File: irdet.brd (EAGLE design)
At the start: 50.8 x 47.9 mm, 66 parts, among them IC1 MEGA8-AI, IC2 78L05F, J1 PSH02-04WG, J2 PSH02-04WG, J3 PSH02-04WG, J4 PSH02-04WG, J5 22-05-7098-09, T1 S9013, T2 S9012, T3 S9013, T4 S9012, T5 S9013, T6 S9012, T7 S9013, T8 S9012, X1 ARK500/2

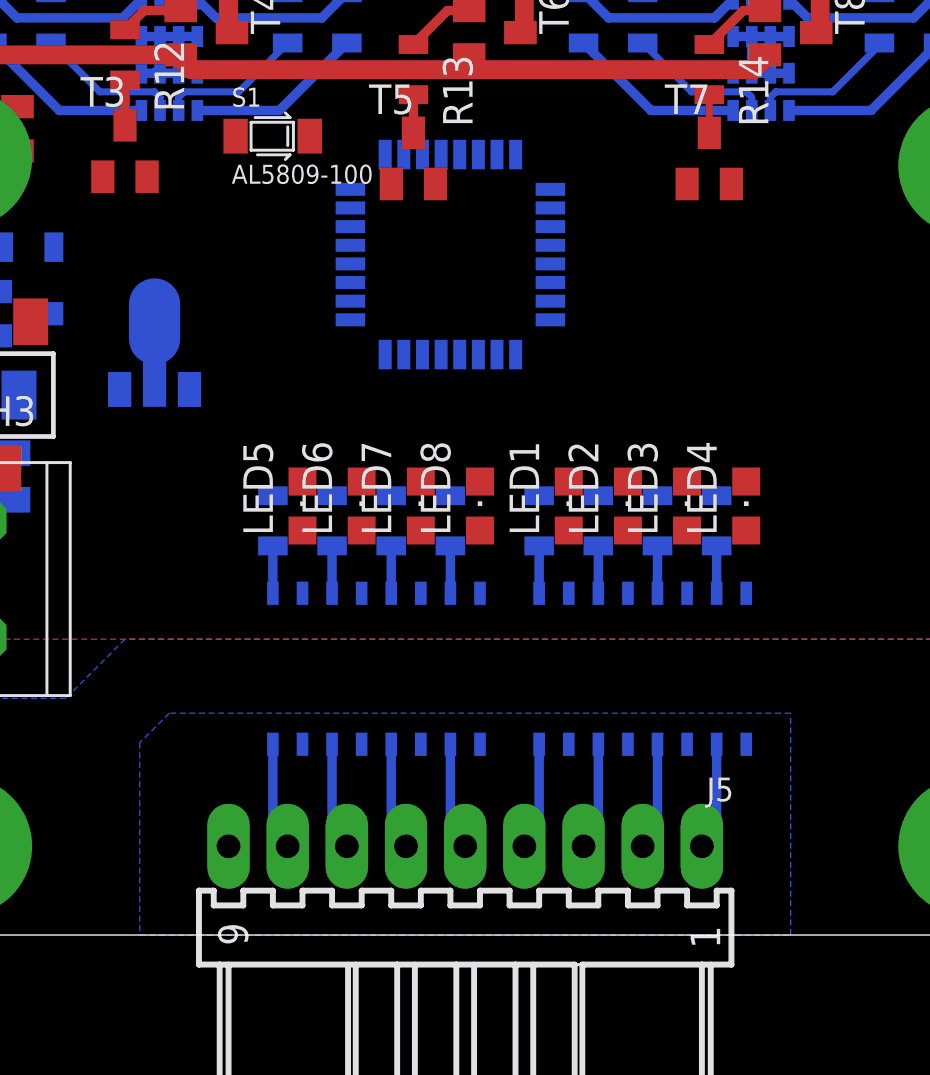
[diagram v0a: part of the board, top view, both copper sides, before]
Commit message: Rotate CPU.
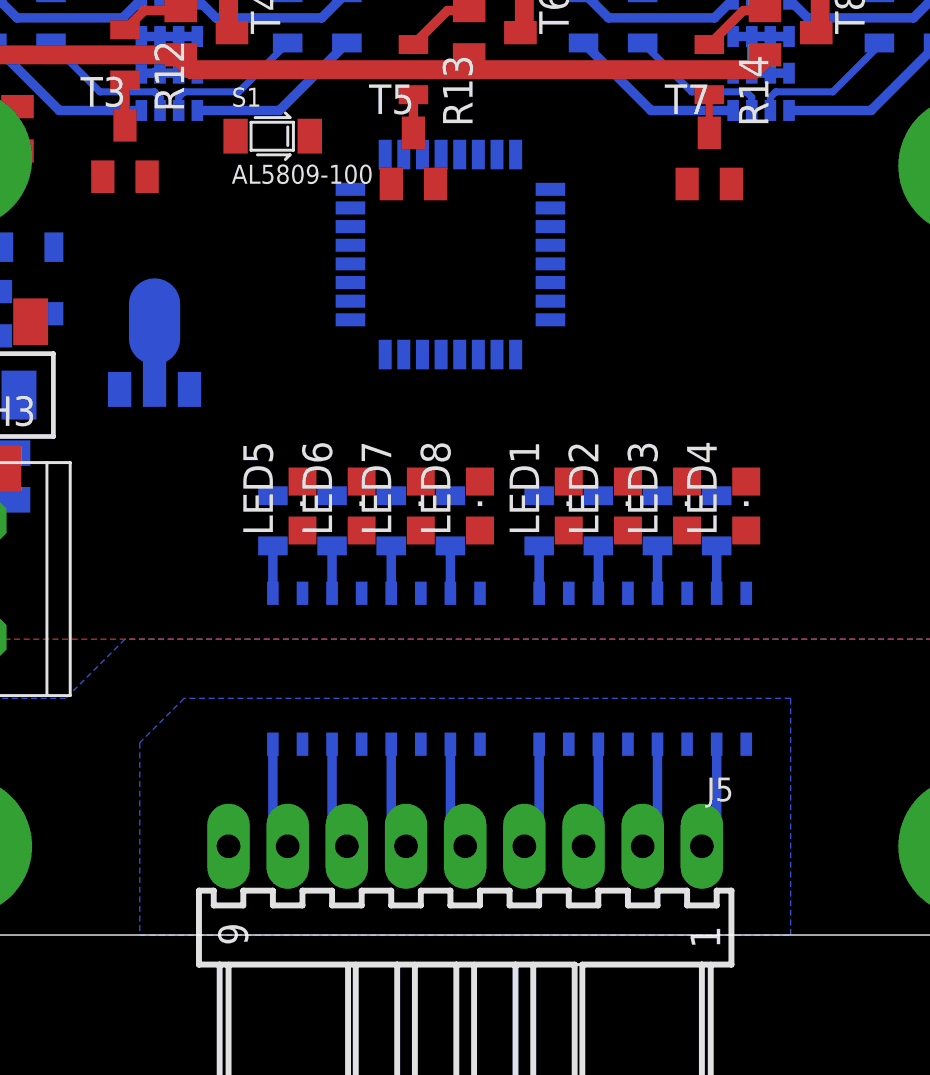
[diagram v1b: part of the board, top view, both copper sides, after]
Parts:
- turned IC1 to 0 degrees

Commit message: Add rest of PCB.
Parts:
- removed C3: 100n, rcl:C0805
- added X2: ARK500/2, con-malina:ARK500/2
- moved ISP1 43.8 mm to (39.4, 24.8), turned to 90 degrees
- moved R1 42.7 mm to (34.6, 27.9), flipped to the bottom, turned to 270 degrees
- moved C2 39.6 mm to (32.4, 27.9), flipped to the bottom, turned to 270 degrees
- moved C16 27.2 mm to (14.0, 28.9), turned to 180 degrees
- moved C1 24.3 mm to (18.4, 27.0), flipped to the bottom, turned to 270 degrees
- moved C8 15.3 mm to (7.94, 14.3), turned to 270 degrees
- moved C7 12.8 mm to (7.94, 18.1), turned to 270 degrees
- moved R2 9.55 mm to (11.7, 27.0), turned to 270 degrees
- moved TH3 9.38 mm to (12.7, 18.7)
- moved IC2 8.28 mm to (12.7, 17.1), turned to 90 degrees
- moved C13 7.73 mm to (9.84, 27.0), turned to 90 degrees
- moved T3 7.24 mm to (17.8, 31.8)
- moved R11 6.36 mm to (7.94, 34.3), turned to 315 degrees
- moved T1 6.11 mm to (10.5, 31.8), turned to 0 degrees
- moved C12 6.03 mm to (3.17, 25.7), turned to 0 degrees
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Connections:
- removed net MISO: IC1.16, ISP1.1
- removed net MOSI/IN7: C14.1, IC1.15, ISP1.4, RN4.2
- removed net N$34: F1.1, X1.1
- removed net OUT1: IC1.30, R3.1
- removed net OUT2: IC1.31, R4.1
- new net +12VIN: F1.1, X1.2, X2.1
- new net IN7: C14.1, IC1.32, RN4.2
- new net MISO/OUT1: IC1.16, ISP1.1, R7.1
- new net MOSI/OUT2: IC1.15, ISP1.4, R8.1
- net +5V: no longer C3.1
- net CPUPOW1-2: now also IC1.23; no longer IC1.12
- net CPUPOW3-4: now also IC1.24; no longer IC1.13
- net CPUPOW5-6: now also IC1.2; no longer IC1.14
- net GND: now also X1.1, X2.2; no longer C3.2, X1.2
- net IN1: now also IC1.25; no longer IC1.23
- net IN2: now also IC1.26; no longer IC1.24
- net IN3: now also IC1.28; no longer IC1.25
- net IN4: now also IC1.27; no longer IC1.26
- net IN5: now also IC1.31; no longer IC1.27
- net IN6: now also IC1.30; no longer IC1.28
- net IN8: now also IC1.1; no longer IC1.8
- net OUT3: now also IC1.14, R9.1; no longer IC1.32, R5.1
- net OUT4: now also IC1.13, R10.1; no longer IC1.1, R6.1
- net OUT5: now also IC1.12, R3.1; no longer IC1.2, R7.1
- net OUT6: now also IC1.11, R4.1; no longer IC1.9, R8.1
- net OUT7: now also R5.1; no longer R9.1
- net OUT8: now also IC1.9, R6.1; no longer IC1.11, R10.1
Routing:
- net +5V: track 12.8 -> 99.1 mm, vias 0 -> 8
- net +12VIN: track 0.00 -> 56.0 mm
- net MOSI/OUT2: track 0.00 -> 25.7 mm, vias 0 -> 1
- net MISO/OUT1: track 0.00 -> 25.2 mm, vias 0 -> 1
- net +12V: track 0.00 -> 24.8 mm, vias 0 -> 1
- net RST: track 0.00 -> 23.7 mm, vias 0 -> 2
- net SCK: track 0.00 -> 23.0 mm, vias 0 -> 1
- net IN7: track 0.00 -> 17.8 mm
- net IN2: track 6.21 -> 20.9 mm
- net CPUPOW1-2: track 0.00 -> 13.3 mm, vias 0 -> 1
- net IN1: track 7.62 -> 20.7 mm
- net CPUPOW7-8: track 0.00 -> 12.9 mm, vias 0 -> 1
- net IN3: track 6.21 -> 17.6 mm
- net IN8: track 7.62 -> 18.8 mm
- net IN6: track 6.21 -> 16.5 mm
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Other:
- board size 50.8 x 47.9 mm -> 50.8 x 45.4 mm

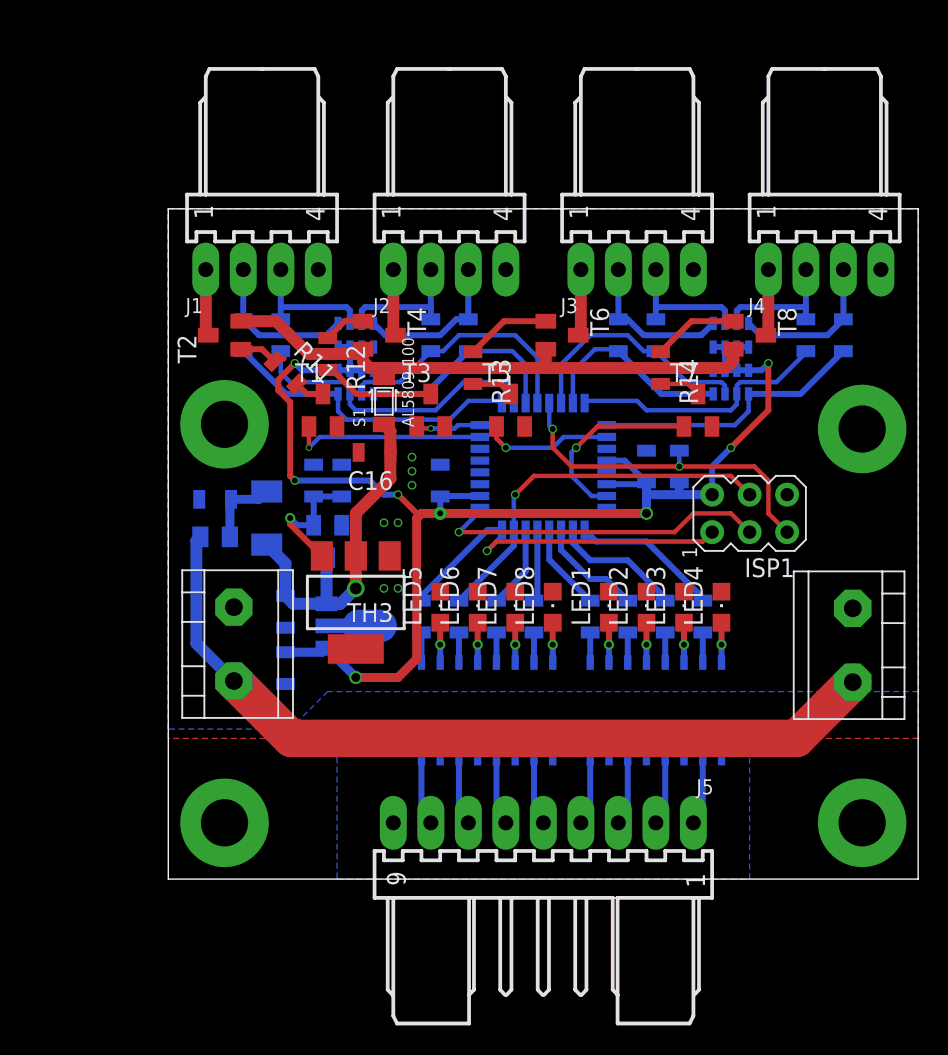
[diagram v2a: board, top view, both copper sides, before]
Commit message: Brd: add texts, position names on silkscreen.
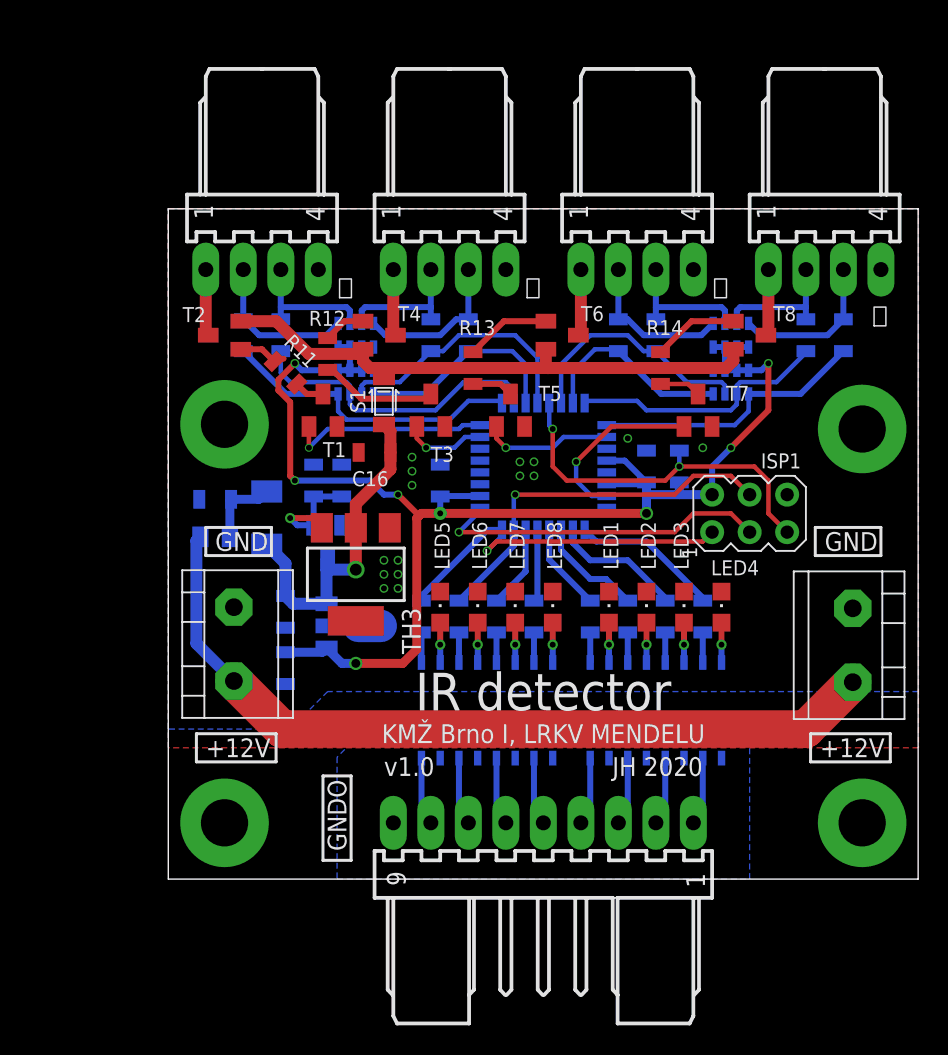
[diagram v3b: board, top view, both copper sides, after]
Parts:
- moved TH3 1.90 mm to (12.7, 20.6)
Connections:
- net CPUPOW1-2: now also IC1.24; no longer IC1.23
- net CPUPOW3-4: now also IC1.23; no longer IC1.24
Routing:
- net RST: track 23.7 -> 25.3 mm
- net +12V: track 24.8 -> 23.4 mm
- net CPUPOW3-4: track 4.42 -> 5.65 mm
- net +5V: track 99.1 -> 97.9 mm
- net N$57: track 9.10 -> 8.07 mm
- net CPUPOW7-8: track 12.9 -> 12.1 mm
- net +12VIN: track 56.0 -> 55.5 mm
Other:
- board text added: "+12V"
- board text added: "GND"
- board text added: "GNDO"
- board text added: "IR detector"
- board text added: "JH 2020"
- board text added: "KMŽ Brno I, LRKV MENDELU"
- board text added: "v1.0"
- board text added: "⏚"

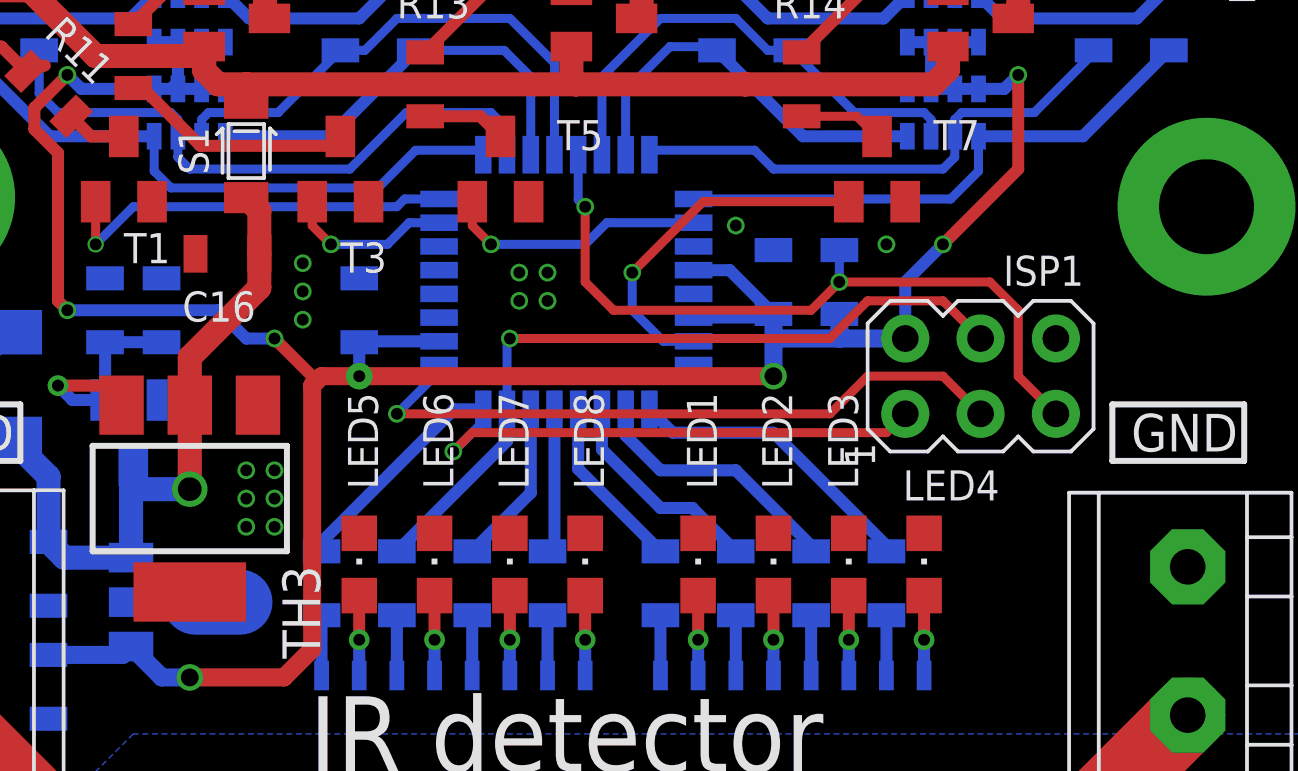
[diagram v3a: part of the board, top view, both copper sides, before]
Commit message: Fix parts names.
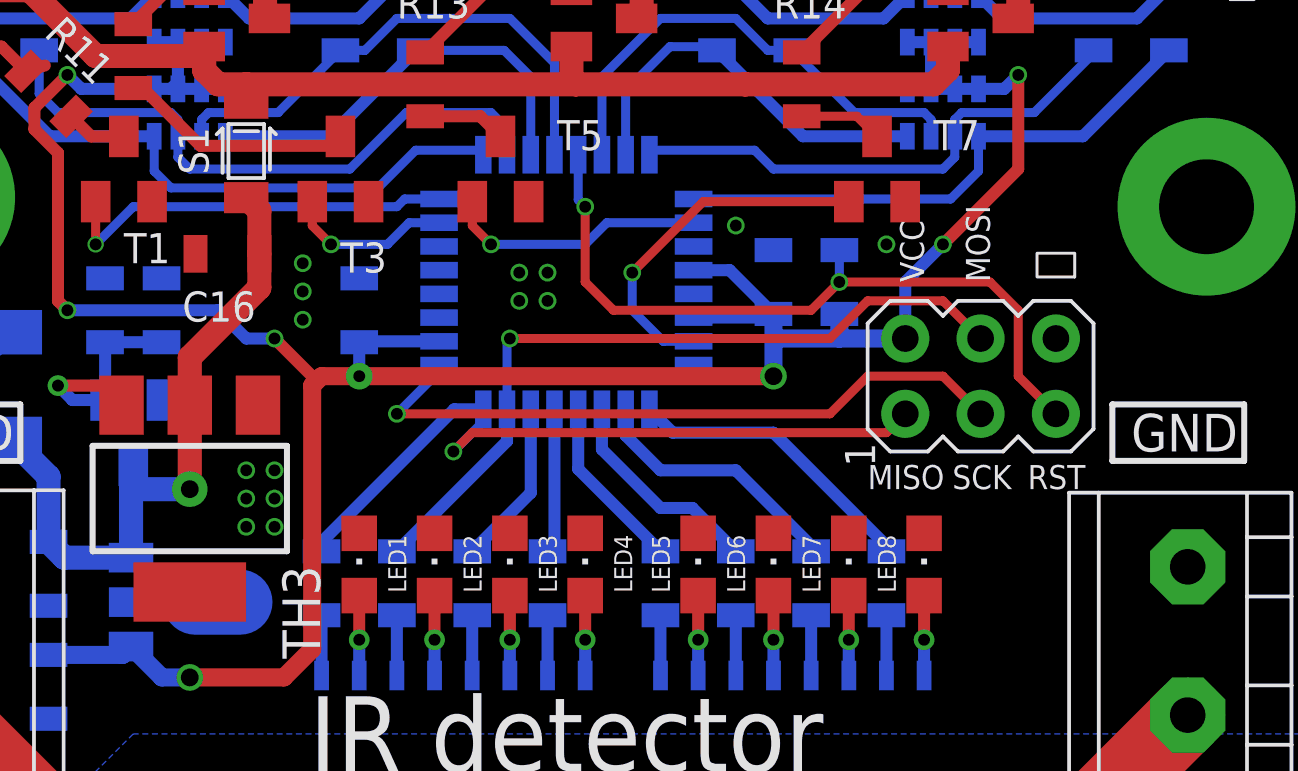
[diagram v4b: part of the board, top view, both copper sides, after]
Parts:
- moved LED4 11.4 mm to (26.0, 18.4)
- moved LED8 11.4 mm to (37.5, 18.4)
- moved OK1 11.4 mm to (21.6, 11.4)
- moved OK2 11.4 mm to (33.0, 11.4)
- moved LED1 11.4 mm to (18.4, 18.4)
- moved LED2 11.4 mm to (21.0, 18.4)
- moved LED5 11.4 mm to (29.8, 18.4)
- moved LED6 11.4 mm to (32.4, 18.4)
- moved LED3 11.4 mm to (23.5, 18.4)
- moved LED7 11.4 mm to (34.9, 18.4)
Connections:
- net N$10: now also OK2.1; no longer OK1.1
- net N$11: now also OK2.7; no longer OK1.7
- net N$12: now also OK2.5; no longer OK1.5
- net N$14: now also OK2.3; no longer OK1.3
- net N$19: now also OK1.1; no longer OK2.1
- net N$20: now also OK1.7; no longer OK2.7
- net N$21: now also OK1.5; no longer OK2.5
- net N$22: now also OK1.3; no longer OK2.3
- net N$26: now also OK2.10; no longer OK1.10
- net N$27: now also OK2.12; no longer OK1.12
- net N$28: now also OK2.14; no longer OK1.14
- net N$29: now also OK2.16; no longer OK1.16
- net N$30: now also OK1.14; no longer OK2.14
- net N$31: now also OK1.16; no longer OK2.16
- net N$32: now also OK1.12; no longer OK2.12
- net N$33: now also OK1.10; no longer OK2.10
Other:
- board text added: "MISO"
- board text added: "MOSI"
- board text added: "RST"
- board text added: "SCK"
- board text added: "VCC"

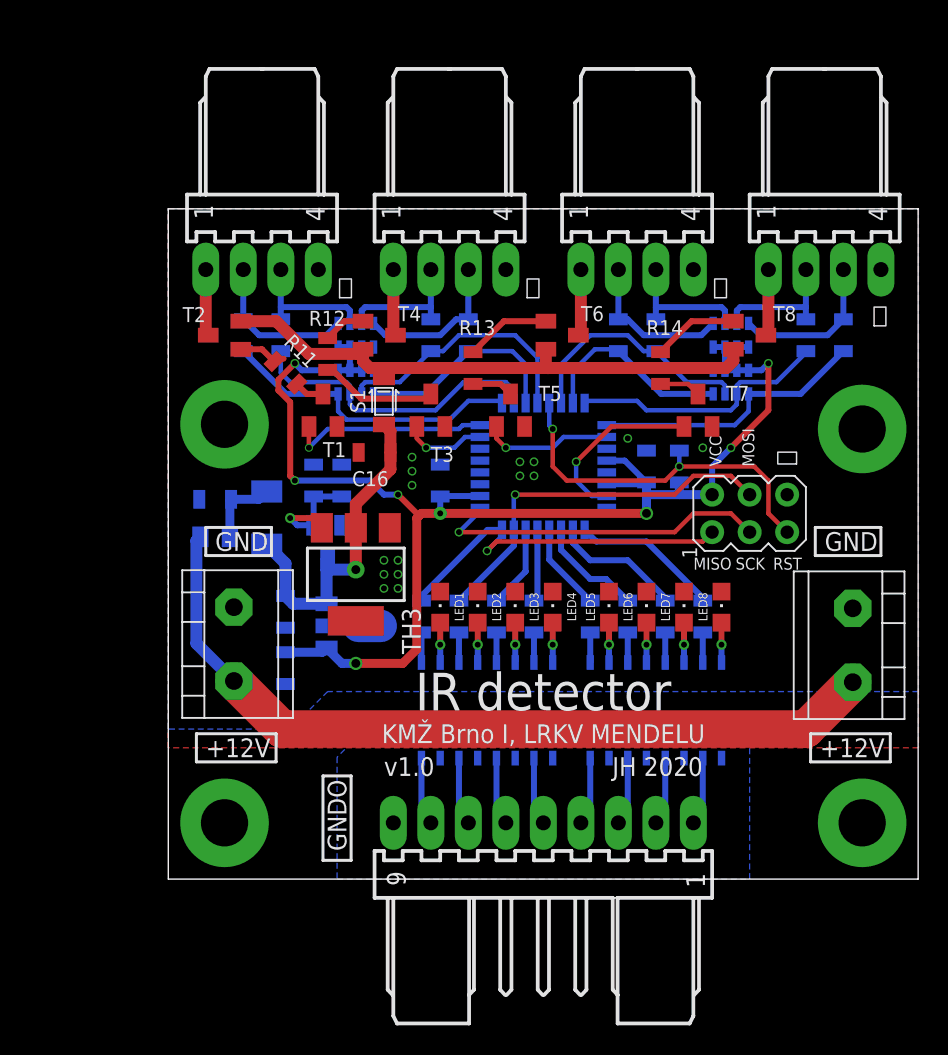
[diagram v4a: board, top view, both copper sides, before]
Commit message: Brd: add round corners.
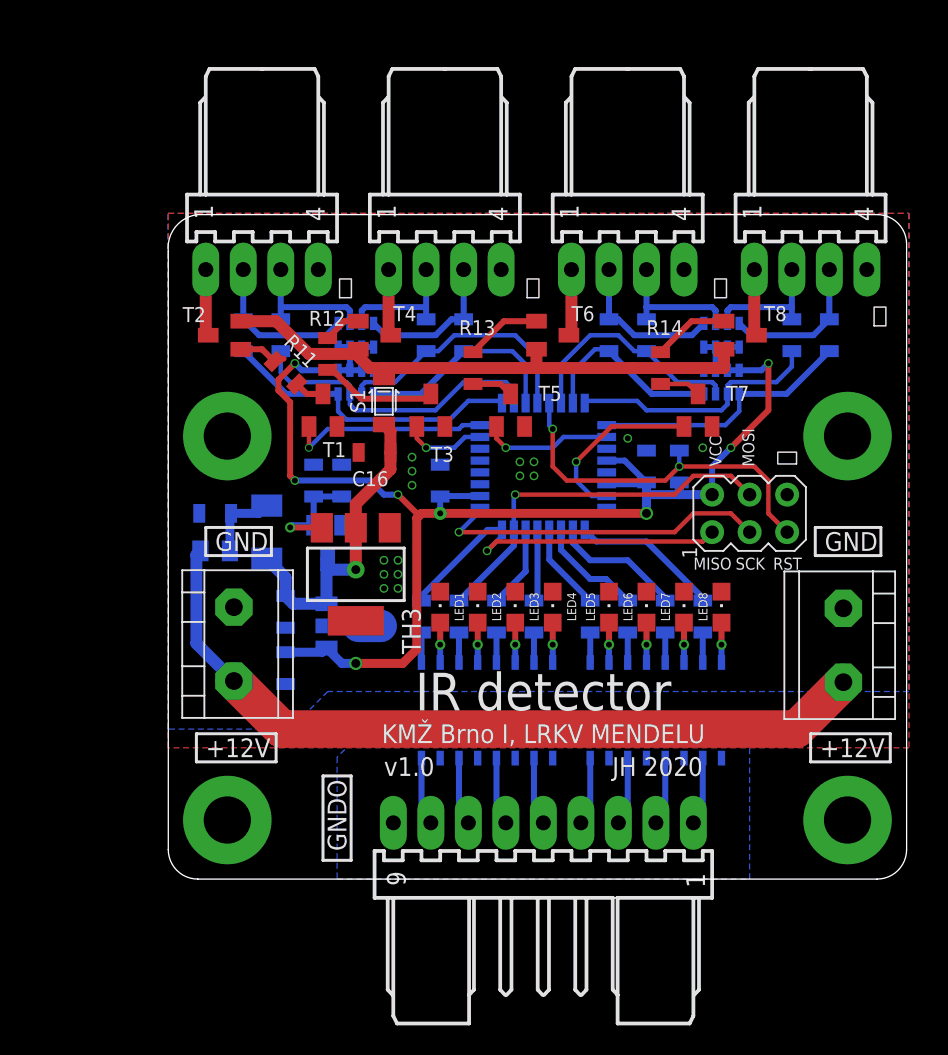
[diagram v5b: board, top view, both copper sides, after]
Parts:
- moved C12 0.95 mm to (3.17, 24.8)
- moved C14 0.95 mm to (42.2, 36.8)
- moved C15 0.95 mm to (44.8, 36.8)
- moved D3 0.95 mm to (6.67, 23.5)
- moved J4 0.95 mm to (43.5, 41.3)
- moved F1 0.95 mm to (3.17, 22.2)
- moved C10 0.64 mm to (32.4, 36.8)
- moved C11 0.64 mm to (29.8, 36.8)
- moved J3 0.64 mm to (31.1, 41.3)
- moved T6 0.64 mm to (26.0, 36.8)
- moved RN3 0.63 mm to (37.5, 36.8)
- moved RN4 0.63 mm to (37.5, 33.7)
- moved T8 0.63 mm to (38.7, 36.8)
- moved X2 0.63 mm to (45.7, 13.3)
- moved C6 0.32 mm to (17.5, 36.8)
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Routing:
- net +12VIN: track 55.5 -> 53.9 mm
- net IN8: track 18.8 -> 17.8 mm
- net +12V: track 23.4 -> 22.5 mm
- net N$40: track 5.80 -> 5.17 mm
- net N$38: track 5.80 -> 5.17 mm
- net IN6: track 16.5 -> 15.9 mm
- net IN5: track 13.5 -> 12.9 mm
- net +5V: track 97.9 -> 98.5 mm
- net N$42: track 38.4 -> 37.8 mm
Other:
- board size 50.8 x 45.4 mm -> 50 x 45 mm
